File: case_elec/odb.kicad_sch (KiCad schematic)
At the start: 9 parts, among them J1 Screw_Terminal_01x02, J2 Conn_02x07_Top_Bottom, SW1 SW_SPST, SW2 SW_SPST, U1 REYAX RYLR896, U2 BNO055, U3 MPL3115A, U4 Ultimate_GPS, U5 Teensy3.5

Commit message: Mise à jour du pcb
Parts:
- J2: footprint (none) -> Connector_Molex:Molex_Nano-Fit_105310-xx14_2x07_P2.50mm_Vertical
- SW2: footprint (none) -> common_misc:SW
- U1: footprint (none) -> Reyax:RYLR896
- U2: footprint (none) -> Adafruit_sensors:BNO055
- U3: footprint (none) -> Adafruit_sensors:MPL3115A2
- U4: footprint (none) -> Adafruit_sensors:Ultimate_GPS
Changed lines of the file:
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@@
       (effects (font (size 1.27 1.27)) (justify right))
     )
-    (property "Footprint" "" (id 2) (at 156.21 166.37 0)
+    (property "Footprint" "Connector_Molex:Molex_Nano-Fit_105310-xx14_2x07_P2.50mm_Vertical" (id 2) (at 156.21 166.37 0)
       (effects (font (size 1.27 1.27)) hide)
     )
@@
     (property "Reference" "U2" (id 0) (at 88.9 99.06 0))
     (property "Value" "BNO055" (id 1) (at 88.9 96.52 0))
-    (property "Footprint" "" (id 2) (at 96.52 93.98 0)
+    (property "Footprint" "Adafruit_sensors:BNO055" (id 2) (at 96.52 93.98 0)
       (effects (font (size 1.27 1.27)) hide)
     )
@@
     (property "Reference" "U4" (id 0) (at 119.38 30.48 0))
     (property "Value" "Ultimate_GPS" (id 1) (at 120.65 33.02 0))
-    (property "Footprint" "" (id 2) (at 113.665 35.56 0)
+    (property "Footprint" "Adafruit_sensors:Ultimate_GPS" (id 2) (at 113.665 35.56 0)
       (effects (font (size 1.27 1.27)) hide)
     )
@@
     (property "Reference" "U1" (id 0) (at 58.42 123.19 0))
     (property "Value" "REYAX RYLR896" (id 1) (at 58.42 125.73 0))
-    (property "Footprint" "" (id 2) (at 59.69 123.19 0)
+    (property "Footprint" "Reyax:RYLR896" (id 2) (at 59.69 123.19 0)
       (effects (font (size 1.27 1.27)) hide)
     )
@@
     (property "Reference" "SW2" (id 0) (at 86.36 123.19 0))
     (property "Value" "SW_SPST" (id 1) (at 86.36 125.73 0))
-    (property "Footprint" "" (id 2) (at 86.36 129.54 0)
+    (property "Footprint" "common_misc:SW" (id 2) (at 86.36 129.54 0)
       (effects (font (size 1.27 1.27)) hide)
     )
@@
     (property "Reference" "U3" (id 0) (at 89.535 69.85 0))
     (property "Value" "MPL3115A" (id 1) (at 89.535 67.31 0))
-    (property "Footprint" "" (id 2) (at 97.79 59.69 0)
+    (property "Footprint" "Adafruit_sensors:MPL3115A2" (id 2) (at 97.79 59.69 0)
       (effects (font (size 1.27 1.27)) hide)
     )
@@
     )
     (path "/55cf5624-44da-424d-9e40-f56e6ab73601"
-      (reference "J2") (unit 1) (value "Conn_02x07_Top_Bottom") (footprint "")
+      (reference "J2") (unit 1) (value "Conn_02x07_Top_Bottom") (footprint "Connector_Molex:Molex_Nano-Fit_105310-xx14_2x07_P2.50mm_Vertical")
     )
     (path "/9077b56f-c102-47b4-9a60-c432e96c7e85"
@@
     )
     (path "/c068de85-ccf9-478f-b6ba-b78ea8eb0dbf"
-      (reference "SW2") (unit 1) (value "SW_SPST") (footprint "")
+      (reference "SW2") (unit 1) (value "SW_SPST") (footprint "common_misc:SW")
     )
     (path "/9723626b-2488-483d-ac8f-0c4da911e062"
-      (reference "U1") (unit 1) (value "REYAX RYLR896") (footprint "")
+      (reference "U1") (unit 1) (value "REYAX RYLR896") (footprint "Reyax:RYLR896")
     )
     (path "/595afb03-5142-4518-8068-322873960ff6"
-      (reference "U2") (unit 1) (value "BNO055") (footprint "")
+      (reference "U2") (unit 1) (value "BNO055") (footprint "Adafruit_sensors:BNO055")
     )
     (path "/dce04994-4869-4e0d-8e66-d9270f6eb7e1"
-      (reference "U3") (unit 1) (value "MPL3115A") (footprint "")
+      (reference "U3") (unit 1) (value "MPL3115A") (footprint "Adafruit_sensors:MPL3115A2")
     )
     (path "/857fdb2b-599c-415c-9c78-a5968f20db3d"
-      (reference "U4") (unit 1) (value "Ultimate_GPS") (footprint "")
+      (reference "U4") (unit 1) (value "Ultimate_GPS") (footprint "Adafruit_sensors:Ultimate_GPS")
     )
     (path "/6dbf9b0b-d170-42c2-945f-d4ad0c4354aa"

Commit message: ajout des librairies teensy
N.B. : chacun devra l'ajouter dans son gestionnaire de librairie, global de préférence
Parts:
- U5: footprint (none) -> teensy:Teensy35_36
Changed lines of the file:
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@@
       (effects (font (size 1.524 1.524)))
     )
-    (property "Footprint" "" (id 2) (at 177.8 31.75 0)
-      (effects (font (size 1.524 1.524)))
+    (property "Footprint" "teensy:Teensy35_36" (id 2) (at 177.8 31.75 0)
+      (effects (font (size 1.524 1.524)) hide)
     )
     (property "Datasheet" "https://www.pjrc.com/teensy/card8a_rev2.pdf" (id 3) (at 180.34 26.67 0)
@@
     )
     (path "/6dbf9b0b-d170-42c2-945f-d4ad0c4354aa"
-      (reference "U5") (unit 1) (value "Teensy3.5") (footprint "")
-    )
-  )
+      (reference "U5") (unit 1) (value "Teensy3.5") (footprint "teensy:Teensy35_36")
+    )
+  )

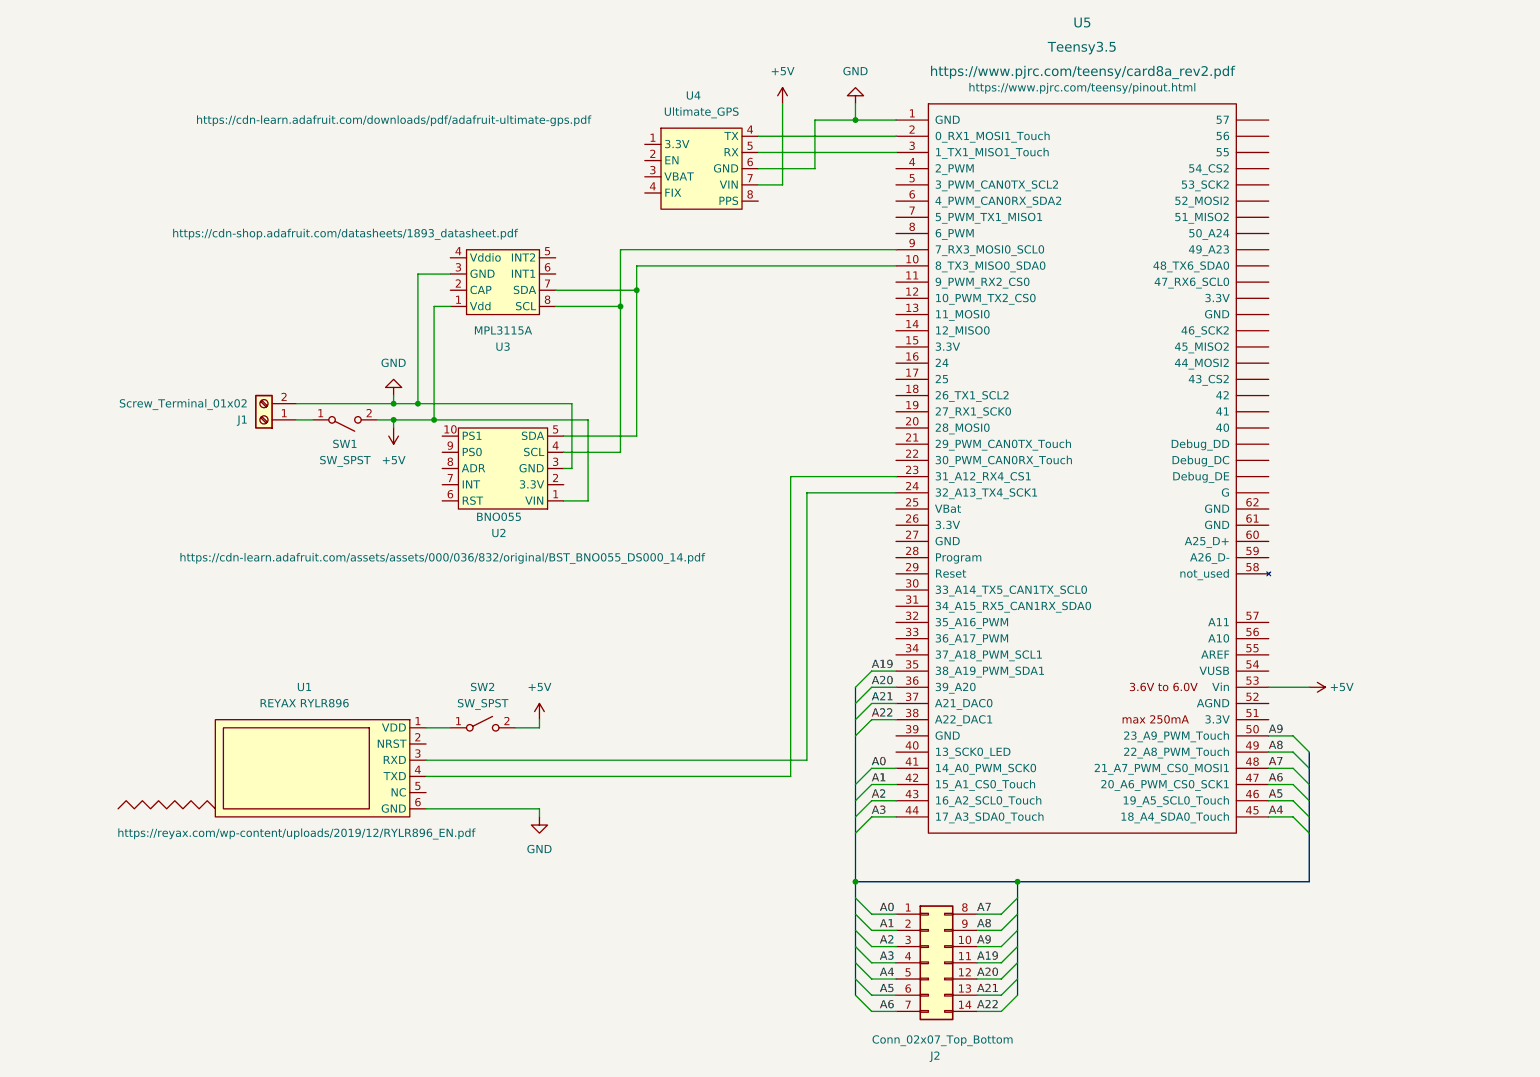
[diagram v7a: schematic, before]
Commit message: agencement approximatif des composants du pcb
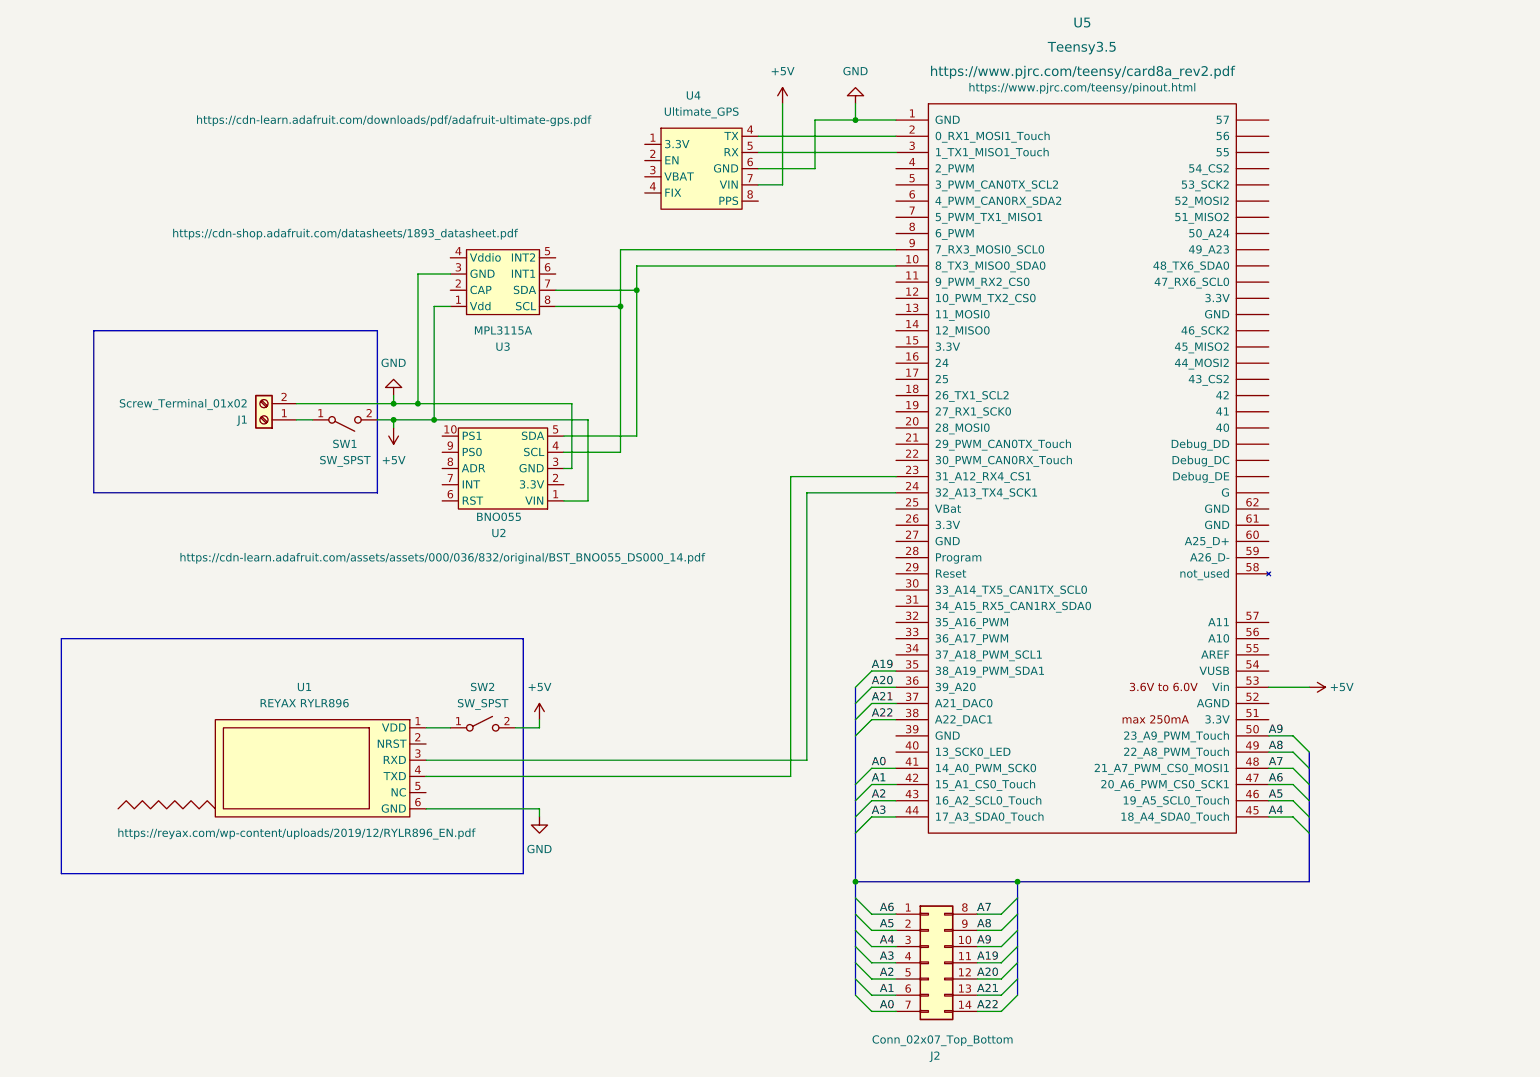
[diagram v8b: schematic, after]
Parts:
- J1: footprint (none) -> TerminalBlock_Phoenix:TerminalBlock_Phoenix_MKDS-1,5-2-5.08_1x02_P5.08mm_Horizontal
- SW1: footprint (none) -> common_misc:SW
- U1: footprint Reyax:RYLR896 -> reyax:RYLR896
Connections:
- net A0: now also J2.7 (Pin_7); no longer J2.1 (Pin_1)
- net A1: now also J2.6 (Pin_6); no longer J2.2 (Pin_2)
- net A2: now also J2.5 (Pin_5); no longer J2.3 (Pin_3)
- net A4: now also J2.3 (Pin_3); no longer J2.5 (Pin_5)
- net A5: now also J2.2 (Pin_2); no longer J2.6 (Pin_6)
- net A6: now also J2.1 (Pin_1); no longer J2.7 (Pin_7)
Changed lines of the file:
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@@
+    (stroke (width 0) (type default) (color 0 0 0 0))
+  )
+  (polyline (pts (xy 20.32 115.57) (xy 92.71 115.57))
     (stroke (width 0) (type default) (color 0 0 0 0))
   )
@@
     (stroke (width 0) (type default) (color 0 0 0 0))
   )
+  (polyline (pts (xy 92.71 115.57) (xy 92.71 152.4))
+    (stroke (width 0) (type default) (color 0 0 0 0))
+  )
   (wire (pts (xy 147.32 128.27) (xy 151.13 128.27))
     (stroke (width 0) (type default) (color 0 0 0 0))
@@
     (stroke (width 0) (type default) (color 0 0 0 0))
   )
+  (polyline (pts (xy 69.85 67.31) (xy 69.85 92.71))
+    (stroke (width 0) (type default) (color 0 0 0 0))
+  )
   (wire (pts (xy 100.33 88.9) (xy 100.33 78.74))
     (stroke (width 0) (type default) (color 0 0 0 0))
@@
     (stroke (width 0) (type default) (color 0 0 0 0))
   )
+  (polyline (pts (xy 25.4 92.71) (xy 25.4 67.31))
+    (stroke (width 0) (type default) (color 0 0 0 0))
+  )
+  (polyline (pts (xy 92.71 152.4) (xy 20.32 152.4))
+    (stroke (width 0) (type default) (color 0 0 0 0))
+  )
   (wire (pts (xy 129.54 36.83) (xy 151.13 36.83))
     (stroke (width 0) (type default) (color 0 0 0 0))
@@
     (stroke (width 0) (type default) (color 0 0 0 0))
   )
+  (polyline (pts (xy 25.4 67.31) (xy 26.67 67.31))
+    (stroke (width 0) (type default) (color 0 0 0 0))
+  )
   (wire (pts (xy 91.44 129.54) (xy 95.25 129.54))
     (stroke (width 0) (type default) (color 0 0 0 0))
@@
     (stroke (width 0) (type default) (color 0 0 0 0))
   )
+  (polyline (pts (xy 26.67 67.31) (xy 69.85 67.31))
+    (stroke (width 0) (type default) (color 0 0 0 0))
+  )
   (bus (pts (xy 144.78 146.05) (xy 144.78 153.67))
     (stroke (width 0) (type default) (color 0 0 0 0))
@@
     (stroke (width 0) (type default) (color 0 0 0 0))
   )
+  (polyline (pts (xy 69.85 92.71) (xy 25.4 92.71))
+    (stroke (width 0) (type default) (color 0 0 0 0))
+  )
   (wire (pts (xy 81.28 63.5) (xy 78.74 63.5))
     (stroke (width 0) (type default) (color 0 0 0 0))
@@
     (stroke (width 0) (type default) (color 0 0 0 0))
   )
+  (polyline (pts (xy 20.32 115.57) (xy 20.32 152.4))
+    (stroke (width 0) (type default) (color 0 0 0 0))
+  )
   (wire (pts (xy 72.39 81.28) (xy 78.74 81.28))
     (stroke (width 0) (type default) (color 0 0 0 0))
@@
     (stroke (width 0) (type default) (color 0 0 0 0))
   )
-  (label "A1" (at 148.59 161.29 0)
+  (label "A4" (at 148.59 163.83 0)
+    (effects (font (size 1.27 1.27)) (justify left bottom))
+  )
+  (label "A5" (at 148.59 161.29 0)
     (effects (font (size 1.27 1.27)) (justify left bottom))
   )
@@
     (effects (font (size 1.27 1.27)) (justify left bottom))
   )
-  (label "A5" (at 148.59 171.45 0)
-    (effects (font (size 1.27 1.27)) (justify left bottom))
-  )
   (label "A19" (at 163.83 166.37 0)
     (effects (font (size 1.27 1.27)) (justify left bottom))
@@
     (effects (font (size 1.27 1.27)) (justify left bottom))
   )
+  (label "A1" (at 148.59 171.45 0)
+    (effects (font (size 1.27 1.27)) (justify left bottom))
+  )
   (label "A1" (at 147.32 138.43 0)
     (effects (font (size 1.27 1.27)) (justify left bottom))
   )
-  (label "A2" (at 148.59 163.83 0)
-    (effects (font (size 1.27 1.27)) (justify left bottom))
-  )
   (label "A21" (at 163.83 171.45 0)
     (effects (font (size 1.27 1.27)) (justify left bottom))
   )
+  (label "A2" (at 148.59 168.91 0)
+    (effects (font (size 1.27 1.27)) (justify left bottom))
+  )
   (label "A6" (at 209.55 138.43 0)
     (effects (font (size 1.27 1.27)) (justify left bottom))
   )
-  (label "A6" (at 148.59 173.99 0)
-    (effects (font (size 1.27 1.27)) (justify left bottom))
-  )
   (label "A0" (at 147.32 135.89 0)
     (effects (font (size 1.27 1.27)) (justify left bottom))
   )
+  (label "A9" (at 163.83 163.83 0)
+    (effects (font (size 1.27 1.27)) (justify left bottom))
+  )
+  (label "A3" (at 148.59 166.37 0)
+    (effects (font (size 1.27 1.27)) (justify left bottom))
+  )
+  (label "A20" (at 163.83 168.91 0)
+    (effects (font (size 1.27 1.27)) (justify left bottom))
+  )
+  (label "A0" (at 148.59 173.99 0)
+    (effects (font (size 1.27 1.27)) (justify left bottom))
+  )
+  (label "A2" (at 147.32 140.97 0)
+    (effects (font (size 1.27 1.27)) (justify left bottom))
+  )
+  (label "A8" (at 209.55 133.35 0)
+    (effects (font (size 1.27 1.27)) (justify left bottom))
+  )
+  (label "A5" (at 209.55 140.97 0)
+    (effects (font (size 1.27 1.27)) (justify left bottom))
+  )
+  (label "A19" (at 147.32 120.65 0)
+    (effects (font (size 1.27 1.27)) (justify left bottom))
+  )
+  (label "A21" (at 147.32 125.73 0)
+    (effects (font (size 1.27 1.27)) (justify left bottom))
+  )
+  (label "A6" (at 148.59 158.75 0)
+    (effects (font (size 1.27 1.27)) (justify left bottom))
+  )
   (label "A7" (at 163.83 158.75 0)
-    (effects (font (size 1.27 1.27)) (justify left bottom))
-  )
-  (label "A20" (at 163.83 168.91 0)
-    (effects (font (size 1.27 1.27)) (justify left bottom))
-  )
-  (label "A2" (at 147.32 140.97 0)
-    (effects (font (size 1.27 1.27)) (justify left bottom))
-  )
-  (label "A8" (at 209.55 133.35 0)
-    (effects (font (size 1.27 1.27)) (justify left bottom))
-  )
-  (label "A5" (at 209.55 140.97 0)
-    (effects (font (size 1.27 1.27)) (justify left bottom))
-  )
-  (label "A19" (at 147.32 120.65 0)
-    (effects (font (size 1.27 1.27)) (justify left bottom))
-  )
-  (label "A21" (at 147.32 125.73 0)
-    (effects (font (size 1.27 1.27)) (justify left bottom))
-  )
-  (label "A3" (at 148.59 166.37 0)
-    (effects (font (size 1.27 1.27)) (justify left bottom))
-  )
-  (label "A0" (at 148.59 158.75 0)
-    (effects (font (size 1.27 1.27)) (justify left bottom))
-  )
-  (label "A9" (at 163.83 163.83 0)
-    (effects (font (size 1.27 1.27)) (justify left bottom))
-  )
-  (label "A4" (at 148.59 168.91 0)
     (effects (font (size 1.27 1.27)) (justify left bottom))
   )
@@
       (effects (font (size 1.27 1.27)) (justify left))
     )
-    (property "Footprint" "" (id 2) (at 52.07 81.28 0)
+    (property "Footprint" "TerminalBlock_Phoenix:TerminalBlock_Phoenix_MKDS-1,5-2-5.08_1x02_P5.08mm_Horizontal" (id 2) (at 52.07 81.28 0)
       (effects (font (size 1.27 1.27)) hide)
     )
@@
     (property "Reference" "SW1" (id 0) (at 64.77 85.09 0))
     (property "Value" "SW_SPST" (id 1) (at 64.77 87.63 0))
-    (property "Footprint" "" (id 2) (at 64.77 81.28 0)
+    (property "Footprint" "common_misc:SW" (id 2) (at 64.77 81.28 0)
       (effects (font (size 1.27 1.27)) hide)
     )
@@
     (property "Reference" "U1" (id 0) (at 58.42 123.19 0))
     (property "Value" "REYAX RYLR896" (id 1) (at 58.42 125.73 0))
-    (property "Footprint" "Reyax:RYLR896" (id 2) (at 59.69 123.19 0)
+    (property "Footprint" "reyax:RYLR896" (id 2) (at 59.69 123.19 0)
       (effects (font (size 1.27 1.27)) hide)
     )
@@
     )
     (path "/650d3695-8ed6-4e36-8fb9-d0029581dc6d"
-      (reference "J1") (unit 1) (value "Screw_Terminal_01x02") (footprint "")
+      (reference "J1") (unit 1) (value "Screw_Terminal_01x02") (footprint "TerminalBlock_Phoenix:TerminalBlock_Phoenix_MKDS-1,5-2-5.08_1x02_P5.08mm_Horizontal")
     )
     (path "/55cf5624-44da-424d-9e40-f56e6ab73601"
@@
     )
     (path "/9077b56f-c102-47b4-9a60-c432e96c7e85"
-      (reference "SW1") (unit 1) (value "SW_SPST") (footprint "")
+      (reference "SW1") (unit 1) (value "SW_SPST") (footprint "common_misc:SW")
     )
     (path "/c068de85-ccf9-478f-b6ba-b78ea8eb0dbf"
@@
     )
     (path "/9723626b-2488-483d-ac8f-0c4da911e062"
-      (reference "U1") (unit 1) (value "REYAX RYLR896") (footprint "Reyax:RYLR896")
+      (reference "U1") (unit 1) (value "REYAX RYLR896") (footprint "reyax:RYLR896")
     )
     (path "/595afb03-5142-4518-8068-322873960ff6"
